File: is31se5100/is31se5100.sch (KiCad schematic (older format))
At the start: 1046 parts

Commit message: Changed i2c pins to open collector
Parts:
- removed D?: B5819W, symbol Device:D_Schottky_Small
- added J1: Conn_01x01, symbol Connector_Generic:Conn_01x01
- added J2, J6: Screw_Terminal_01x02, symbol Connector:Screw_Terminal_01x02
- added J3: USB_B_Micro, symbol Connector:USB_B_Micro
- added JP1: SolderJumper_3_Bridged12, symbol Jumper:SolderJumper_3_Bridged12
- F1, F2: renamed from F?; value 250mA -> 1A
- gave numbers to parts that had none: 1043
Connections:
- net labels removed: 5V_CTRL, GND1, GND_CTRL, MC_INTERRUPT
- wire segments 684 -> 695
- no-connect marks 1228 -> 1248
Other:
- note added: "Control"
- note added: "Extraneous parts"
- note added: "INTB is an interrupt line that is open drain\n (I beileve it is open drain)"
- note added: "SPI Tinker"
- note removed: "INTB is an interrupt line that is open drain"
- moved on the sheet: C1, C10, C100, C101, C102, C103, C104, C105, C106, C107, C108, C109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

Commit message: Added more debug jumpers to test the open drain of INTB pins of IS31SE5100
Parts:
- removed JP1: SolderJumper_3_Bridged12, symbol Jumper:SolderJumper_3_Bridged12
- removed R1: 10k, symbol Device:R_Small
- removed R86: 2k2, symbol Device:R_Small
- added H1, H2, H3, H4: MountingHole_Pad, symbol Mechanical:MountingHole_Pad
- added J? (x7): Conn_01x01, symbol Connector_Generic:Conn_01x01
- added JP? (x7): SolderJumper_3_Bridged12, symbol Jumper:SolderJumper_3_Bridged12
- added R? (x2): 4k7, symbol Device:R_Small
- renumbered JP2 to JP1, JP11 to JP10, JP12 to JP11, JP13 to JP12, JP14 to JP13, JP15 to JP14, JP16 to JP15, JP17 to JP16, JP3 to JP2, JP4 to JP3, JP5 to JP4, JP6 to JP5, JP7 to JP6, JP8 to JP7, JP9 to JP8, JP10 to JP9
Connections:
- net +3V3: now also R?.1
- net GND: now also H1.1, H2.1, H3.1, H4.1
- net INTB1: now also JP?.2 (C); no longer U26.17 (INTB), U27.17 (INTB), U55.17 (INTB), U56.17 (INTB), U57.17 (INTB)
- net INTB_CTRL: now also JP?.2 (C)
- net at J1.1 (Pin_1): now also JP?.1 (A), JP?.1 (A), JP?.1 (A), JP?.1 (A), JP?.1 (A), JP?.1 (A), R?.2
- net at R84.1: now also R85.1
- new net: J?.1 (Pin_1), JP?.3 (B) (x7)
- new net: JP?.1 (A), R?.2
- new net INTB2: JP?.2 (C), U26.17 (INTB)
- new net INTB3: JP?.2 (C), U27.17 (INTB)
- new net INTB4: JP?.2 (C), U57.17 (INTB)
- new net INTB5: JP?.2 (C), U55.17 (INTB)
- new net INTB6: JP?.2 (C), U56.17 (INTB)
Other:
- moved on the sheet: J1, J6

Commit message: Confirmed schematic
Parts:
- removed J4: Conn_01x04, symbol Connector_Generic:Conn_01x04
- added C100, C101, C102, C103, C104, C105, C98, C99: 3pF3, symbol Device:C_Small
- added C82, C83, C84, C85, C86, C87, C88, C89: 3pF, symbol Device:C_Small
- added C90, C91, C92, C93, C94, C95, C96, C97: 12pF, symbol Device:C_Small
- added J10: Conn_01x05, symbol Connector_Generic:Conn_01x05
- added JP7: SolderJumper_3_Bridged12, symbol Jumper:SolderJumper_3_Bridged12
- gave numbers to parts that had none: 16
- renumbered C82 to C106, C83 to C107, C84 to C108, C85 to C109, C86 to C110, C87 to C111, C88 to C112, C89 to C113, C90 to C114, C91 to C115, C92 to C116, C93 to C117, C94 to C118, C95 to C119, C96 to C120, C97 to C121, C98 to C122, C99 to C123, C100 to C124, C101 to C125, C102 to C126, C103 to C127, C104 to C128, C105 to C129, C106 to C130, C107 to C131, C108 to C132, C109 to C133, C110 to C134, C111 to C135, C112 to C136, C113 to C137, C114 to C138, C115 to C139, C116 to C140, C117 to C141, C118 to C142, C119 to C143, C120 to C144, C121 to C145, C122 to C146, C123 to C147, C124 to C148, C125 to C149, C126 to C150, C127 to C151, C128 to C152, C129 to C153, C130 to C154, C131 to C155, C132 to C156, C133 to C157, C134 to C158, C135 to C159, C136 to C160, C137 to C161, C138 to C162, C139 to C163, C140 to C164, C141 to C165, C142 to C166, C143 to C167, C144 to C168, C145 to C169, C146 to C170, C147 to C171, C148 to C172, C149 to C173, C150 to C174, C151 to C175, C152 to C176, C153 to C177, C154 to C178, C155 to C179, C156 to C180, C157 to C181, C158 to C182, C159 to C183, C160 to C184, C161 to C185, C162 to C186, C163 to C187, C164 to C188, C165 to C189, C166 to C190, C167 to C191, C168 to C192, C169 to C193, C170 to C194, C171 to C195, C172 to C196, C173 to C197, C174 to C198, C175 to C199, C176 to C200, C177 to C201, C178 to C202, C179 to C203, C180 to C204, C181 to C205, C182 to C206, C183 to C207, C184 to C208, C185 to C209, C186 to C210, C187 to C211, C188 to C212, C189 to C213, C190 to C214, C191 to C215, C192 to C216, C193 to C217, C194 to C218, C195 to C219, C196 to C220, C197 to C221, C198 to C222, C199 to C223, C200 to C224, C201 to C225, C202 to C226, C203 to C227, C204 to C228, C205 to C229, C206 to C230, C207 to C231, C208 to C232, C209 to C233, C210 to C234, C211 to C235, C212 to C236, C213 to C237, C214 to C238, C215 to C239, C216 to C240, C217 to C241, C218 to C242, C219 to C243, C220 to C244, C221 to C245, C222 to C246, C223 to C247, C224 to C248, C225 to C249, C226 to C250, C227 to C251, C228 to C252, C229 to C253, C230 to C254, C231 to C255, C232 to C256, C233 to C257, C234 to C258, C235 to C259, C236 to C260, C237 to C261, C238 to C262, C239 to C263, C240 to C264, C241 to C265, J5 to J11, J6 to J12, J8 to J13, J9 to J14, J10 to J15, J7 to J16, J11 to J18, J12 to J19, J13 to J20, J14 to J21, J15 to J22, J16 to J23, J17 to J24, J18 to J25, J19 to J26, J20 to J27, J21 to J28, J22 to J29, J23 to J30, J2 to J8, J3 to J9, JP3 to JP10, JP4 to JP11, JP5 to JP12, JP6 to JP13, JP7 to JP14, JP8 to JP15, JP9 to JP17, JP10 to JP18, JP11 to JP19, JP12 to JP20, JP13 to JP21, JP14 to JP22, JP15 to JP23, JP16 to JP24, JP1 to JP8, JP2 to JP9
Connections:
- net DIN: now also J10.3 (Pin_3)
- net DIN_CTRL: now also J27.3 (Pin_3); no longer J27.2 (Pin_2)
- net DOUT: now also J10.4 (Pin_4)
- net DOUT_CTRL: now also J27.4 (Pin_4); no longer J27.1 (Pin_1)
- net INTB_CTRL: now also J16.3 (Pin_3); no longer J16.1 (Pin_1)
- net SCKL: now also J10.2 (Pin_2)
- net SCKL_CTRL: now also J27.2 (Pin_2); no longer J27.3 (Pin_3)
- net SCL_CTRL: now also J16.1 (Pin_1); no longer J16.3 (Pin_3)
- net ~CS: now also J10.1 (Pin_1)
- net ~CS_CTRL: now also J27.1 (Pin_1); no longer J27.4 (Pin_4)
- net at U58.4 (DOUT): now also JP7.2 (C); no longer U59.34 (DIN)
- new net: JP7.1 (A), U59.34 (DIN)
- new net DOUT_SINGLE: J10.5 (Pin_5), JP7.3 (B)
- no-connect marks 1248 -> 1296
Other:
- moved on the sheet: C106, C107, C108, C109, C110, C111, C112, C113, C114, C115, C116, C117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

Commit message: Rename schematic parts
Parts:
- removed C100, C101, C102, C103, C104, C105, C99: 3pF3, symbol Device:C_Small
- removed C107, C108, C109, C110, C111, C112, C113: 1pF, symbol Device:C_Small
- removed C115, C116, C117, C118, C119, C120, C121: 5pF, symbol Device:C_Small
- removed C123, C124, C125, C126, C127, C128, C129: 10pF, symbol Device:C_Small
- removed C131, C132, C133, C134, C135, C136, C137: 15pF, symbol Device:C_Small
- removed C139, C140, C141, C142, C143, C144, C145: 1nF, symbol Device:C_Small
- removed C147, C148, C149, C150, C151, C152, C153: 5nF, symbol Device:C_Small
- removed C155, C156, C157, C158, C159, C160, C161: 10nF, symbol Device:C_Small
- removed C163, C164, C165, C166, C167, C168, C169: 15nF, symbol Device:C_Small
- removed C171, C172, C173, C174, C175, C176, C177: 25nF, symbol Device:C_Small
- removed C179, C180, C181, C182, C183, C184, C185: 50nF, symbol Device:C_Small
- removed C187, C188, C189, C190, C191, C192, C193: 100nF, symbol Device:C_Small
- removed C195, C196, C197, C198, C199, C200, C201: 1uF, symbol Device:C_Small
- removed C203, C204, C205, C206, C207, C208, C209: 5uF, symbol Device:C_Small
- removed C211, C212, C213, C214, C215, C216, C217: 10uF, symbol Device:C_Small
- removed C219, C220, C221, C222, C223, C224, C225: 15uF, symbol Device:C_Small
- removed C227, C228, C229, C230, C231, C232, C233: 25uF, symbol Device:C_Small
- removed C235, C236, C237, C238, C239, C240, C241: 50uF, symbol Device:C_Small
- removed C243, C244, C245, C246, C247, C248, C249: 18pF, symbol Device:C_Small
- removed C251, C252, C253, C254, C255, C256, C257: 20pF, symbol Device:C_Small
- removed C259, C260, C261, C262, C263, C264, C265: 22pF, symbol Device:C_Small
- removed C83, C84, C85, C86, C87, C88, C89: 3pF, symbol Device:C_Small
- removed C91, C92, C93, C94, C95, C96, C97: 12pF, symbol Device:C_Small
- removed R112, R113, R114, R115, R116, R117, R118: 1, symbol Device:R_Small
- removed R120, R121, R122, R123, R124, R125, R126: 10, symbol Device:R_Small
- removed R128, R129, R130, R131, R132, R133, R134: 100, symbol Device:R_Small
- removed R136, R137, R138, R139, R140, R141, R142: 1k, symbol Device:R_Small
- removed R144, R145, R146, R147, R148, R149, R150: 10k, symbol Device:R_Small
- removed R152, R153, R154, R155, R156, R157, R158: 100k, symbol Device:R_Small
- removed R160, R161, R162, R163, R164, R165, R166: 1.5, symbol Device:R_Small
- removed R168, R169, R170, R171, R172, R173, R174: 15, symbol Device:R_Small
- removed R176, R177, R178, R179, R180, R181, R182: 150, symbol Device:R_Small
- removed R184, R185, R186, R187, R188, R189, R190: 1k5, symbol Device:R_Small
- removed R192, R193, R194, R195, R196, R197, R198: 15k, symbol Device:R_Small
- removed R200, R201, R202, R203, R204, R205, R206: 150k, symbol Device:R_Small
- removed R208, R209, R210, R211, R212, R213, R214: 2.2, symbol Device:R_Small
- removed R216, R217, R218, R219, R220, R221, R222: 22, symbol Device:R_Small
- removed R224, R225, R226, R227, R228, R229, R230: 220, symbol Device:R_Small
- removed R232, R233, R234, R235, R236, R237, R238: 2k2, symbol Device:R_Small
- removed R240, R241, R242, R243, R244, R245, R246: 22k, symbol Device:R_Small
- removed R248, R249, R250, R251, R252, R253, R254: 220k, symbol Device:R_Small
- removed R256, R257, R258, R259, R260, R261, R262: 2.7, symbol Device:R_Small
- removed R264, R265, R266, R267, R268, R269, R270: 27, symbol Device:R_Small
- removed R272, R273, R274, R275, R276, R277, R278: 270, symbol Device:R_Small
- removed R280, R281, R282, R283, R284, R285, R286: 2k7, symbol Device:R_Small
- removed R288, R289, R290, R291, R292, R293, R294: 27k, symbol Device:R_Small
- removed R296, R297, R298, R299, R300, R301, R302: 270k, symbol Device:R_Small
- removed R304, R305, R306, R307, R308, R309, R310: 3.3, symbol Device:R_Small
- removed R312, R313, R314, R315, R316, R317, R318: 33, symbol Device:R_Small
- removed R320, R321, R322, R323, R324, R325, R326: 330, symbol Device:R_Small
- removed R328, R329, R330, R331, R332, R333, R334: 3k3, symbol Device:R_Small
- removed R336, R337, R338, R339, R340, R341, R342: 33k, symbol Device:R_Small
- removed R344, R345, R346, R347, R348, R349, R350: 330k, symbol Device:R_Small
- removed R352, R353, R354, R355, R356, R357, R358: 3.9, symbol Device:R_Small
- removed R360, R361, R362, R363, R364, R365, R366: 39, symbol Device:R_Small
- removed R368, R369, R370, R371, R372, R373, R374: 390, symbol Device:R_Small
- removed R376, R377, R378, R379, R380, R381, R382: 3k9, symbol Device:R_Small
- removed R384, R385, R386, R387, R388, R389, R390: 39k, symbol Device:R_Small
- removed R392, R393, R394, R395, R396, R397, R398: 390k, symbol Device:R_Small
- removed R400, R401, R402, R403, R404, R405, R406: 4.7, symbol Device:R_Small
- removed R408, R409, R410, R411, R412, R413, R414: 47, symbol Device:R_Small
- removed R416, R417, R418, R419, R420, R421, R422: 470, symbol Device:R_Small
- removed R424, R425, R426, R427, R428, R429, R430: 4k7, symbol Device:R_Small
- removed R432, R433, R434, R435, R436, R437, R438: 47k, symbol Device:R_Small
- removed R440, R441, R442, R443, R444, R445, R446: 470k, symbol Device:R_Small
- removed R448, R449, R450, R451, R452, R453, R454: 5.1, symbol Device:R_Small
- removed R456, R457, R458, R459, R460, R461, R462: 51, symbol Device:R_Small
- removed R464, R465, R466, R467, R468, R469, R470: 510, symbol Device:R_Small
- removed R472, R473, R474, R475, R476, R477, R478: 5k1, symbol Device:R_Small
- removed R480, R481, R482, R483, R484, R485, R486: 51k, symbol Device:R_Small
- removed R488, R489, R490, R491, R492, R493, R494: 510k, symbol Device:R_Small
- removed R496, R497, R498, R499, R500, R501, R502: 120, symbol Device:R_Small
- removed R504, R505, R506, R507, R508, R509, R510: 180, symbol Device:R_Small
- removed R512, R513, R514, R515, R516, R517, R518: 250, symbol Device:R_Small
- removed R520, R521, R522, R523, R524, R525, R526: 300, symbol Device:R_Small
- removed R528, R529, R530, R531, R532, R533, R534: 360, symbol Device:R_Small
- removed R536, R537, R538, R539, R540, R541, R542: 430, symbol Device:R_Small
- removed R544, R545, R546, R547, R548, R549, R550: 1M, symbol Device:R_Small
- removed R552, R553, R554, R555, R556, R557, R558: 0, symbol Device:R_Small
- added CX10, CX11, CX12, CX13, CX14, CX15, CX16: 12pF, symbol Device:C_Small
- added CX100, CX101, CX102, CX103, CX104, CX98, CX99: 50nF, symbol Device:C_Small
- added CX106, CX107, CX108, CX109, CX110, CX111, CX112: 100nF, symbol Device:C_Small
- added CX114, CX115, CX116, CX117, CX118, CX119, CX120: 1uF, symbol Device:C_Small
- added CX122, CX123, CX124, CX125, CX126, CX127, CX128: 5uF, symbol Device:C_Small
- added CX130, CX131, CX132, CX133, CX134, CX135, CX136: 10uF, symbol Device:C_Small
- added CX138, CX139, CX140, CX141, CX142, CX143, CX144: 15uF, symbol Device:C_Small
- added CX146, CX147, CX148, CX149, CX150, CX151, CX152: 25uF, symbol Device:C_Small
- added CX154, CX155, CX156, CX157, CX158, CX159, CX160: 50uF, symbol Device:C_Small
- added CX162, CX163, CX164, CX165, CX166, CX167, CX168: 18pF, symbol Device:C_Small
- added CX170, CX171, CX172, CX173, CX174, CX175, CX176: 20pF, symbol Device:C_Small
- added CX178, CX179, CX180, CX181, CX182, CX183, CX184: 22pF, symbol Device:C_Small
- added CX18, CX19, CX20, CX21, CX22, CX23, CX24: 3pF3, symbol Device:C_Small
- added CX2, CX3, CX4, CX5, CX6, CX7, CX8: 3pF, symbol Device:C_Small
- added CX26, CX27, CX28, CX29, CX30, CX31, CX32: 1pF, symbol Device:C_Small
- added CX34, CX35, CX36, CX37, CX38, CX39, CX40: 5pF, symbol Device:C_Small
- added CX42, CX43, CX44, CX45, CX46, CX47, CX48: 10pF, symbol Device:C_Small
- added CX50, CX51, CX52, CX53, CX54, CX55, CX56: 15pF, symbol Device:C_Small
- added CX58, CX59, CX60, CX61, CX62, CX63, CX64: 1nF, symbol Device:C_Small
- added CX66, CX67, CX68, CX69, CX70, CX71, CX72: 5nF, symbol Device:C_Small
- added CX74, CX75, CX76, CX77, CX78, CX79, CX80: 10nF, symbol Device:C_Small
- added CX82, CX83, CX84, CX85, CX86, CX87, CX88: 15nF, symbol Device:C_Small
- added CX90, CX91, CX92, CX93, CX94, CX95, CX96: 25nF, symbol Device:C_Small
- added RX10, RX11, RX12, RX13, RX14, RX15, RX16: 10, symbol Device:R_Small
- added RX100, RX101, RX102, RX103, RX104, RX98, RX99: 2.2, symbol Device:R_Small
- added RX106, RX107, RX108, RX109, RX110, RX111, RX112: 22, symbol Device:R_Small
- added RX114, RX115, RX116, RX117, RX118, RX119, RX120: 220, symbol Device:R_Small
- added RX122, RX123, RX124, RX125, RX126, RX127, RX128: 2k2, symbol Device:R_Small
- added RX130, RX131, RX132, RX133, RX134, RX135, RX136: 22k, symbol Device:R_Small
- added RX138, RX139, RX140, RX141, RX142, RX143, RX144: 220k, symbol Device:R_Small
- added RX146, RX147, RX148, RX149, RX150, RX151, RX152: 2.7, symbol Device:R_Small
- added RX154, RX155, RX156, RX157, RX158, RX159, RX160: 27, symbol Device:R_Small
- added RX162, RX163, RX164, RX165, RX166, RX167, RX168: 270, symbol Device:R_Small
- added RX170, RX171, RX172, RX173, RX174, RX175, RX176: 2k7, symbol Device:R_Small
- added RX178, RX179, RX180, RX181, RX182, RX183, RX184: 27k, symbol Device:R_Small
- added RX18, RX19, RX20, RX21, RX22, RX23, RX24: 100, symbol Device:R_Small
- added RX186, RX187, RX188, RX189, RX190, RX191, RX192: 270k, symbol Device:R_Small
- added RX194, RX195, RX196, RX197, RX198, RX199, RX200: 3.3, symbol Device:R_Small
- added RX2, RX3, RX4, RX5, RX6, RX7, RX8: 1, symbol Device:R_Small
- added RX202, RX203, RX204, RX205, RX206, RX207, RX208: 33, symbol Device:R_Small
- added RX210, RX211, RX212, RX213, RX214, RX215, RX216: 330, symbol Device:R_Small
- added RX218, RX219, RX220, RX221, RX222, RX223, RX224: 3k3, symbol Device:R_Small
- added RX226, RX227, RX228, RX229, RX230, RX231, RX232: 33k, symbol Device:R_Small
- added RX234, RX235, RX236, RX237, RX238, RX239, RX240: 330k, symbol Device:R_Small
- added RX242, RX243, RX244, RX245, RX246, RX247, RX248: 3.9, symbol Device:R_Small
- added RX250, RX251, RX252, RX253, RX254, RX255, RX256: 39, symbol Device:R_Small
- added RX258, RX259, RX260, RX261, RX262, RX263, RX264: 390, symbol Device:R_Small
- added RX26, RX27, RX28, RX29, RX30, RX31, RX32: 1k, symbol Device:R_Small
- added RX266, RX267, RX268, RX269, RX270, RX271, RX272: 3k9, symbol Device:R_Small
- added RX274, RX275, RX276, RX277, RX278, RX279, RX280: 39k, symbol Device:R_Small
- added RX282, RX283, RX284, RX285, RX286, RX287, RX288: 390k, symbol Device:R_Small
- added RX290, RX291, RX292, RX293, RX294, RX295, RX296: 4.7, symbol Device:R_Small
- added RX298, RX299, RX300, RX301, RX302, RX303, RX304: 47, symbol Device:R_Small
- added RX306, RX307, RX308, RX309, RX310, RX311, RX312: 470, symbol Device:R_Small
- added RX314, RX315, RX316, RX317, RX318, RX319, RX320: 4k7, symbol Device:R_Small
- added RX322, RX323, RX324, RX325, RX326, RX327, RX328: 47k, symbol Device:R_Small
- added RX330, RX331, RX332, RX333, RX334, RX335, RX336: 470k, symbol Device:R_Small
- added RX338, RX339, RX340, RX341, RX342, RX343, RX344: 5.1, symbol Device:R_Small
- added RX34, RX35, RX36, RX37, RX38, RX39, RX40: 10k, symbol Device:R_Small
- added RX346, RX347, RX348, RX349, RX350, RX351, RX352: 51, symbol Device:R_Small
- added RX354, RX355, RX356, RX357, RX358, RX359, RX360: 510, symbol Device:R_Small
- added RX362, RX363, RX364, RX365, RX366, RX367, RX368: 5k1, symbol Device:R_Small
- added RX370, RX371, RX372, RX373, RX374, RX375, RX376: 51k, symbol Device:R_Small
- added RX378, RX379, RX380, RX381, RX382, RX383, RX384: 510k, symbol Device:R_Small
- added RX386, RX387, RX388, RX389, RX390, RX391, RX392: 120, symbol Device:R_Small
- added RX394, RX395, RX396, RX397, RX398, RX399, RX400: 180, symbol Device:R_Small
- added RX402, RX403, RX404, RX405, RX406, RX407, RX408: 250, symbol Device:R_Small
- added RX410, RX411, RX412, RX413, RX414, RX415, RX416: 300, symbol Device:R_Small
- added RX418, RX419, RX420, RX421, RX422, RX423, RX424: 360, symbol Device:R_Small
- added RX42, RX43, RX44, RX45, RX46, RX47, RX48: 100k, symbol Device:R_Small
- added RX426, RX427, RX428, RX429, RX430, RX431, RX432: 430, symbol Device:R_Small
- added RX434, RX435, RX436, RX437, RX438, RX439, RX440: 1M, symbol Device:R_Small
- added RX442, RX443, RX444, RX445, RX446, RX447, RX448: 0, symbol Device:R_Small
- added RX50, RX51, RX52, RX53, RX54, RX55, RX56: 1.5, symbol Device:R_Small
- added RX58, RX59, RX60, RX61, RX62, RX63, RX64: 15, symbol Device:R_Small
- added RX66, RX67, RX68, RX69, RX70, RX71, RX72: 150, symbol Device:R_Small
- added RX74, RX75, RX76, RX77, RX78, RX79, RX80: 1k5, symbol Device:R_Small
- added RX82, RX83, RX84, RX85, RX86, RX87, RX88: 15k, symbol Device:R_Small
- added RX90, RX91, RX92, RX93, RX94, RX95, RX96: 150k, symbol Device:R_Small
- renumbered C32 to C31, C33 to C32, C34 to C33, C35 to C34, C36 to C35, C37 to C36, C38 to C37, C39 to C38, C40 to C39, C41 to C40, C42 to C41, C43 to C42, C44 to C43, C45 to C44, C46 to C45, C48 to C46, C49 to C47, C50 to C48, C51 to C49, C52 to C50, C53 to C51, C54 to C52, C55 to C53, C56 to C54, C57 to C55, C58 to C56, C59 to C57, C61 to C58, C62 to C59, C63 to C60, C65 to C61, C66 to C62, C67 to C63, C68 to C64, C69 to C65, C70 to C66, C71 to C67, C72 to C68, C74 to C69, C75 to C70, C76 to C71, C77 to C72, C81 to C73, C31 to CP1, C47 to CP2, C60 to CP3, C64 to CP4, C73 to CP5, C78 to CP6, C79 to CP7, C80 to CP8, C82 to CX1, C186 to CX105, C194 to CX113, C202 to CX121, C210 to CX129, C218 to CX137, C226 to CX145, C234 to CX153, C242 to CX161, C250 to CX169, C98 to CX17, C258 to CX177, C106 to CX25, C114 to CX33, C122 to CX41, C130 to CX49, C138 to CX57, C146 to CX65, C154 to CX73, C162 to CX81, C170 to CX89, C90 to CX9, C178 to CX97, R42 to R40, R46 to R41, R47 to R42, R48 to R43, R49 to R44, R50 to R45, R51 to R46, R52 to R47, R53 to R48, R54 to R49, R55 to R50, R56 to R51, R57 to R52, R58 to R53, R59 to R54, R60 to R55, R61 to R56, R62 to R57, R63 to R58, R64 to R59, R65 to R60, R66 to R61, R67 to R62, R68 to R63, R69 to R64, R70 to R65, R71 to R66, R72 to R67, R73 to R68, R74 to R69, R75 to R70, R76 to R71, R77 to R72, R78 to R73, R79 to R74, R81 to R75, R82 to R76, R83 to R77, R84 to R78, R85 to R79, R86 to R80, R89 to R81, R90 to R82, R91 to R83, R92 to R84, R93 to R85, R94 to R86, R95 to R87, R96 to R88, R97 to R89, R98 to R90, R99 to R91, R103 to R92, R104 to R93, R105 to R94, R106 to R95, R107 to R96, R108 to R97, R110 to R98, R40 to RP1, R101 to RP10, R102 to RP11, R109 to RP12, R41 to RP2, R43 to RP3, R44 to RP4, R45 to RP5, R80 to RP6, R87 to RP7, R88 to RP8, R100 to RP9, R111 to RX1, R215 to RX105, R223 to RX113, R231 to RX121, R239 to RX129, R247 to RX137, R255 to RX145, R263 to RX153, R271 to RX161, R279 to RX169, R127 to RX17, R287 to RX177, R295 to RX185, R303 to RX193, R311 to RX201, R319 to RX209, R327 to RX217, R335 to RX225, R343 to RX233, R351 to RX241, R359 to RX249, R135 to RX25, R367 to RX257, R375 to RX265, R383 to RX273, R391 to RX281, R399 to RX289, R407 to RX297, R415 to RX305, R423 to RX313, R431 to RX321, R439 to RX329, R143 to RX33, R447 to RX337, R455 to RX345, R463 to RX353, R471 to RX361, R479 to RX369, R487 to RX377, R495 to RX385, R503 to RX393, R511 to RX401, R519 to RX409, R151 to RX41, R527 to RX417, R535 to RX425, R543 to RX433, R551 to RX441, R159 to RX49, R167 to RX57, R175 to RX65, R183 to RX73, R191 to RX81, R199 to RX89, R119 to RX9, R207 to RX97

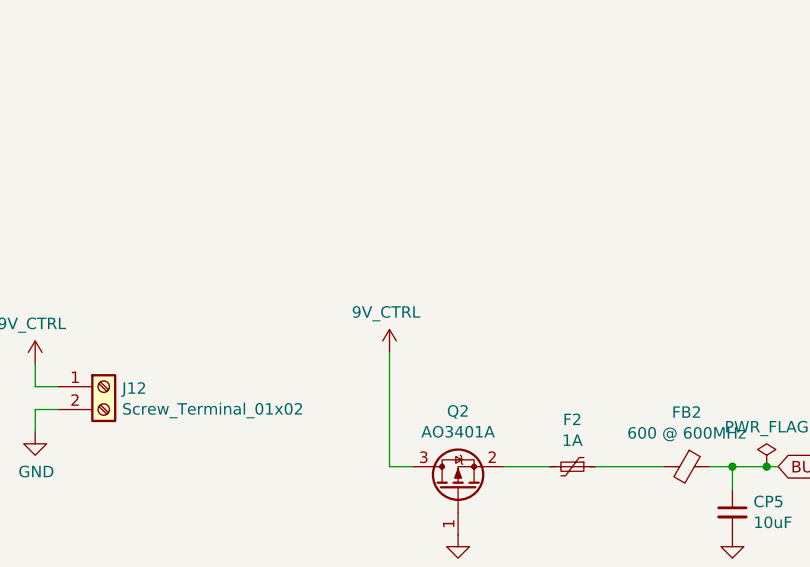
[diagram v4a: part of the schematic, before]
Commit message: Matched footprints for main parts
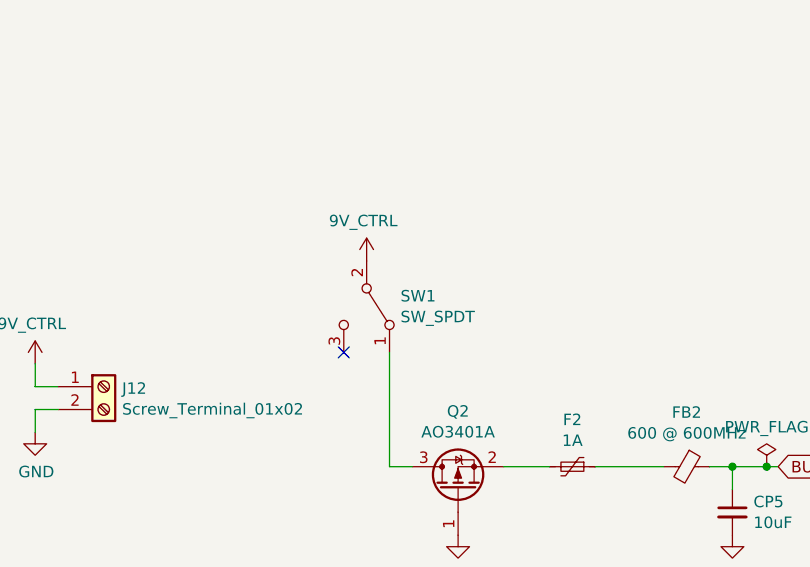
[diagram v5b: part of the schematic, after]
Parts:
- added SW1: SW_SPDT, Button_Switch_SMD:SW_SPDT_PCM12, symbol Switch:SW_SPDT
- C1, C10, C11, C12, C13, C14, C15, C16, C17, C18, C19, C2, C20, C21, C22, C23, C24, C3, C31, C32, C33, C34, C35, C36, C37, C38, C39, C4, C40, C41, C42, C43, C44, C45, C46, C47, C48, C49, C5, C50, C51, C52, C53, C54, C6, C63, C64, C65, C66, C67, C68, C69, C7, C70, C8, C9: footprint (none) -> Capacitor_SMD:C_0603_1608Metric_Pad1.08x0.95mm_HandSolder
- C25, C26, C27, C55, C56, C57, C71: footprint (none) -> Capacitor_SMD:C_0603_1608Metric
- C28, C29, C30, C58, C59, C60, C61, C62, C72, C73: footprint (none) -> Capacitor_SMD:C_0402_1005Metric
- CP1, CP2, CP3, CP4, CP5, CP6, CP7, CP8: footprint (none) -> Capacitor_SMD:C_1206_3216Metric
- D1, D2, D8: footprint (none) -> Diode_SMD:D_SOD-123
- D10, D11, D12, D13, D3, D4, D5, D6, D7, D9: footprint (none) -> LED_SMD:LED_0603_1608Metric
- F1, F2: footprint (none) -> Fuse:Fuse_1206_3216Metric
- FB1, FB2: footprint (none) -> Inductor_SMD:L_0805_2012Metric
- H1, H2, H3, H4: footprint (none) -> MountingHole:MountingHole_3.2mm_M3_Pad_Via
- J1, J17, J2, J3, J4, J5, J6, J7: footprint (none) -> Connector_PinHeader_2.54mm:PinHeader_1x01_P2.54mm_Vertical
- J10: footprint (none) -> Connector_PinHeader_2.54mm:PinHeader_1x05_P2.54mm_Vertical
- J11, J13, J14, J15, J18, J19, J20, J21, J22, J23, J24, J25, J26, J28, J29, J30: footprint (none) -> Connector_PinHeader_2.54mm:PinHeader_1x08_P2.54mm_Vertical
- J12, J8: footprint (none) -> TerminalBlock_Phoenix:TerminalBlock_Phoenix_PT-1,5-2-3.5-H_1x02_P3.50mm_Horizontal
- J16: footprint (none) -> Connector_PinHeader_2.54mm:PinHeader_1x03_P2.54mm_Vertical
- J27: footprint (none) -> Connector_PinHeader_2.54mm:PinHeader_1x04_P2.54mm_Vertical
- J9: footprint (none) -> Connector_USB:USB_Micro-B_Molex_47346-0001
- JP1, JP10, JP11, JP12, JP13, JP14, JP15, JP16, JP17, JP18, JP19, JP2, JP20, JP21, JP22, JP23, JP24, JP3, JP4, JP5, JP6, JP7, JP8, JP9: footprint (none) -> Jumper:SolderJumper-3_P1.3mm_Bridged12_RoundedPad1.0x1.5mm
- L1, L2: footprint (none) -> Inductor_SMD:L_Sunlord_MWSA0518_5.4x5.2mm
- R1, R15, R2, R22, R23, R24, R29, R3, R38, R39, R4, R40, R41, R42, R47, R5, R56, R57, R58, R59, R6, R7, R70, R73, R74, R75, R78, R79, R8, R80, R81, R82, R83, R84, R85, R86, R87, R88, R89, RP1, RP10, RP11, RP12, RP2, RP3, RP4, RP5, RP6, RP7, RP8, RP9: footprint (none) -> Resistor_SMD:R_0603_1608Metric_Pad0.98x0.95mm_HandSolder
- R10, R11, R12, R13, R14, R16, R17, R18, R19, R20, R21, R25, R26, R27, R28, R30, R31, R32, R33, R34, R35, R36, R37, R43, R44, R45, R46, R48, R49, R50, R51, R52, R53, R54, R55, R60, R61, R62, R63, R64, R65, R66, R67, R68, R69, R71, R72, R76, R77, R9, R90, R91, R92, R93, R94, R95, R96, R97, R98: footprint (none) -> Resistor_SMD:R_0603_1608Metric
- U116, U53: footprint (none) -> Package_TO_SOT_SMD:SOT-23-6_Handsoldering
- U117, U26, U27, U28, U55, U56, U57: footprint (none) -> Package_SO:SSOP-24_5.3x8.2mm_P0.65mm
- U190, U58, U59: footprint (none) -> Custom:MAX7301AAX
- U25, U54: footprint (none) -> Package_SO:TSSOP-16_4.4x5mm_P0.65mm
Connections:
- net at Q2.3 (D): now also SW1.1 (A)
- no-connect marks 1296 -> 1297
